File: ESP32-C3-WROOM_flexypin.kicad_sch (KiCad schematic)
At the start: 14 parts, among them J1 Conn_01x09, J19 USB_C_Receptacle_USB2.0_14P, J2 Conn_01x09, J22 Conn_01x09, J3 Conn_01x09, SW1 SW_Push, SW3 SW_Push, U1 RT9080

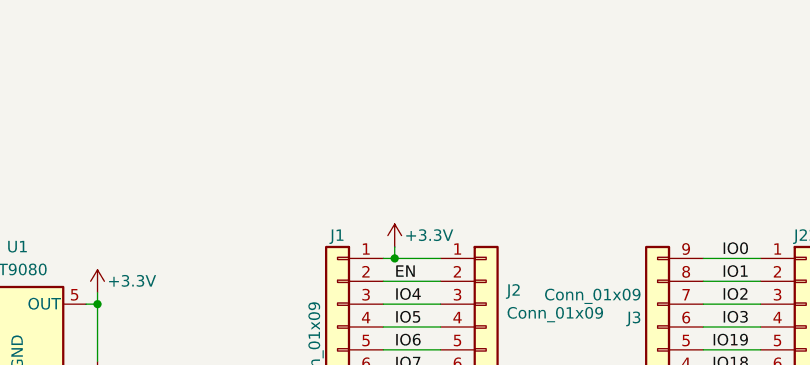
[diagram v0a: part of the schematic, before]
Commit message: added LED
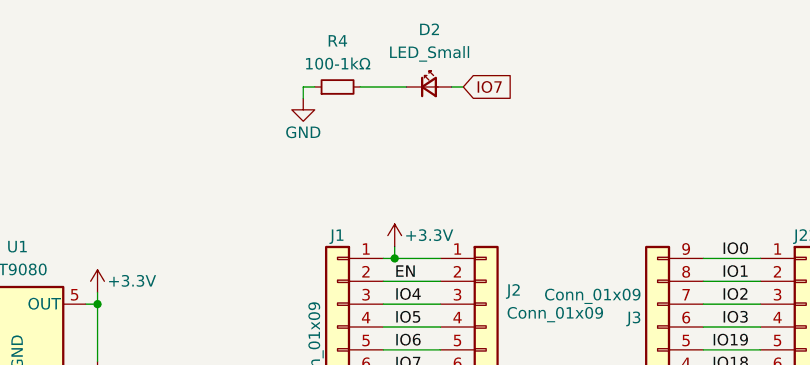
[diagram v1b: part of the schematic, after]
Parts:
- added D2: LED_Small, LED_SMD:LED_0402_1005Metric, symbol Device:LED_Small
- added R4: 100-1kΩ, Resistor_SMD:R_0402_1005Metric, symbol Device:R_Small
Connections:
- net GND: now also R4.1
- net IO7: now also D2.2 (A)
- new net: D2.1 (K), R4.2
